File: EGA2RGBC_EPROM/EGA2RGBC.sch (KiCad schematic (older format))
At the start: 21 parts, among them J1 EGA Input, J3 CSync Selection, J4 Power, J5 Video Out, U1 27C010, U2 74LS244

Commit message: Update schematics
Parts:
- added JP2: Brown Fix, Connector_PinHeader_2.54mm:PinHeader_1x02_P2.54mm_Vertical, symbol Device:Jumper_NO_Small
- added R9: 4.7k, Resistor_THT:R_Axial_DIN0204_L3.6mm_D1.6mm_P7.62mm_Horizontal, symbol Device:R_Small
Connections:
- net GND: now also R9.1; no longer U1.26 (A9)
- net VCC: now also JP2.1
- new net: JP2.2, R9.2, U1.26 (A9)
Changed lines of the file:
@@
 $EndComp
-Wire Wire Line
-	2400 5750 2150 5750
-Wire Wire Line
-	2150 5750 2150 5850
 Wire Wire Line
 	2150 6450 2400 6450
 Wire Wire Line
 	2400 5850 2150 5850
-Connection ~ 2150 5850
 Wire Wire Line
 	2150 5850 2150 5950
@@
 	1    0    0    -1
 $EndComp
+$Comp
+L Device:R_Small R9
+U 1 1 6017B880
+P 1350 5750
+F 0 "R9" V 1400 5850 50  0000 C CNN
+F 1 "4.7k" V 1400 5600 50  0000 C CNN
+F 2 "Resistor_THT:R_Axial_DIN0204_L3.6mm_D1.6mm_P7.62mm_Horizontal" H 1350 5750 50  0001 C CNN
+F 3 "~" H 1350 5750 50  0001 C CNN
+	1    1350 5750
+	0    -1   -1   0
+$EndComp
+$Comp
+L Device:Jumper_NO_Small JP2
+U 1 1 6017DE7E
+P 1700 5950
+F 0 "JP2" H 1400 6050 50  0000 C CNN
+F 1 "Brown Fix" H 1700 6044 50  0000 C CNN
+F 2 "Connector_PinHeader_2.54mm:PinHeader_1x02_P2.54mm_Vertical" H 1700 5950 50  0001 C CNN
+F 3 "~" H 1700 5950 50  0001 C CNN
+	1    1700 5950
+	1    0    0    -1
+$EndComp
+Wire Wire Line
+	1050 4850 1050 5750
+Wire Wire Line
+	1050 5750 1250 5750
+Connection ~ 1050 4850
+Wire Wire Line
+	1450 5750 1950 5750
+Wire Wire Line
+	1800 5950 1950 5950
+Wire Wire Line
+	1950 5950 1950 5750
+Connection ~ 1950 5750
+Wire Wire Line
+	1950 5750 2400 5750
+$Comp
+L power:VCC #PWR?
+U 1 1 601AF6F5
+P 1350 5950
+F 0 "#PWR?" H 1350 5800 50  0001 C CNN
+F 1 "VCC" H 1365 6123 50  0000 C CNN
+F 2 "" H 1350 5950 50  0001 C CNN
+F 3 "" H 1350 5950 50  0001 C CNN
+	1    1350 5950
+	0    -1   -1   0
+$EndComp
+Wire Wire Line
+	1350 5950 1600 5950
 $EndSCHEMATC

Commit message: Create rev 1.1
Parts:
- C4, C5: footprint Capacitor_THT:C_Disc_D6.0mm_W2.5mm_P5.00mm -> Capacitor_THT:C_Disc_D3.0mm_W2.0mm_P2.50mm
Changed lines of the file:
@@
 Title ""
 Date ""
-Rev ""
+Rev "1.1"
 Comp ""
 Comment1 ""
@@
 F 0 "C4" H 6592 4296 50  0000 L CNN
 F 1 "100nF" H 6592 4205 50  0000 L CNN
-F 2 "Capacitor_THT:C_Disc_D6.0mm_W2.5mm_P5.00mm" H 6500 4250 50  0001 C CNN
+F 2 "Capacitor_THT:C_Disc_D3.0mm_W2.0mm_P2.50mm" H 6500 4250 50  0001 C CNN
 F 3 "~" H 6500 4250 50  0001 C CNN
 	1    6500 4250
@@
 F 0 "C5" H 7042 4296 50  0000 L CNN
 F 1 "100nF" H 7042 4205 50  0000 L CNN
-F 2 "Capacitor_THT:C_Disc_D6.0mm_W2.5mm_P5.00mm" H 6950 4250 50  0001 C CNN
+F 2 "Capacitor_THT:C_Disc_D3.0mm_W2.0mm_P2.50mm" H 6950 4250 50  0001 C CNN
 F 3 "~" H 6950 4250 50  0001 C CNN
 	1    6950 4250

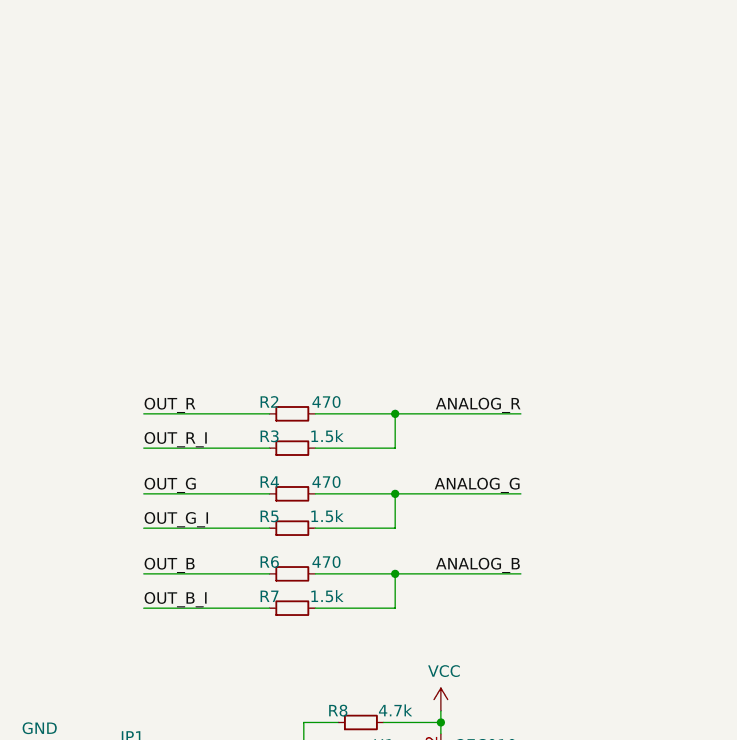
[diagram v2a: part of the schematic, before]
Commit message: Added caps on color lines
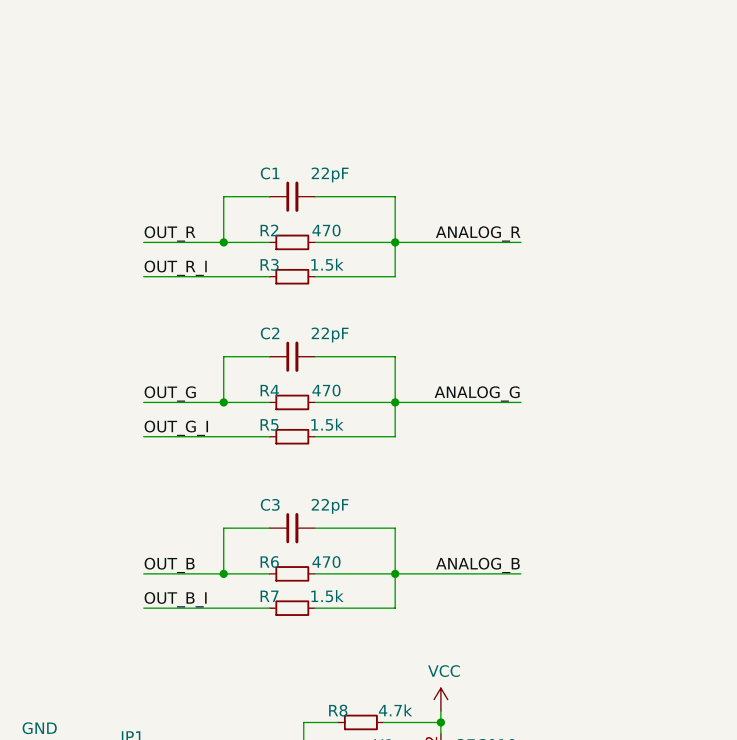
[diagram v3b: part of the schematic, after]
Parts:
- added C1, C2, C3: 22pF, Capacitor_THT:C_Disc_D3.0mm_W2.0mm_P2.50mm, symbol Device:C_Small
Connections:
- net ANALOG_B: now also C3.2
- net ANALOG_G: now also C2.2
- net ANALOG_R: now also C1.2
- net OUT_B: now also C3.1
- net OUT_G: now also C2.1
- net OUT_R: now also C1.1
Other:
- moved on the sheet: R2, R3, R4, R5
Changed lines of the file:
@@
 $EndComp
 Wire Wire Line
-	1500 3250 2050 3250
+	1500 2500 1850 2500
 $Comp
 L Device:R_Small R2
 U 1 1 5FC5E289
-P 2150 3250
-F 0 "R2" V 2200 3350 50  0000 C CNN
-F 1 "470" V 2200 3100 50  0000 C CNN
-F 2 "Resistor_THT:R_Axial_DIN0204_L3.6mm_D1.6mm_P7.62mm_Horizontal" H 2150 3250 50  0001 C CNN
-F 3 "~" H 2150 3250 50  0001 C CNN
-	1    2150 3250
-	0    -1   -1   0
-$EndComp
-Wire Wire Line
-	2250 3250 2600 3250
+P 2150 2500
+F 0 "R2" V 2200 2600 50  0000 C CNN
+F 1 "470" V 2200 2350 50  0000 C CNN
+F 2 "Resistor_THT:R_Axial_DIN0204_L3.6mm_D1.6mm_P7.62mm_Horizontal" H 2150 2500 50  0001 C CNN
+F 3 "~" H 2150 2500 50  0001 C CNN
+	1    2150 2500
+	0    -1   -1   0
+$EndComp
+Wire Wire Line
+	2250 2500 2600 2500
 $Comp
 L Device:R_Small R3
 U 1 1 5FC60558
-P 2150 3400
-F 0 "R3" V 2200 3500 50  0000 C CNN
-F 1 "1.5k" V 2200 3250 50  0000 C CNN
-F 2 "Resistor_THT:R_Axial_DIN0204_L3.6mm_D1.6mm_P7.62mm_Horizontal" H 2150 3400 50  0001 C CNN
-F 3 "~" H 2150 3400 50  0001 C CNN
-	1    2150 3400
-	0    -1   -1   0
-$EndComp
-Wire Wire Line
-	2250 3400 2600 3400
-Wire Wire Line
-	2600 3400 2600 3250
-Connection ~ 2600 3250
-Wire Wire Line
-	2600 3250 3150 3250
-Wire Wire Line
-	2050 3400 1500 3400
-Text Label 1500 3250 0    50   ~ 0
+P 2150 2650
+F 0 "R3" V 2200 2750 50  0000 C CNN
+F 1 "1.5k" V 2200 2500 50  0000 C CNN
+F 2 "Resistor_THT:R_Axial_DIN0204_L3.6mm_D1.6mm_P7.62mm_Horizontal" H 2150 2650 50  0001 C CNN
+F 3 "~" H 2150 2650 50  0001 C CNN
+	1    2150 2650
+	0    -1   -1   0
+$EndComp
+Wire Wire Line
+	2250 2650 2600 2650
+Wire Wire Line
+	2600 2650 2600 2500
+Connection ~ 2600 2500
+Wire Wire Line
+	2600 2500 3150 2500
+Wire Wire Line
+	2050 2650 1500 2650
+Text Label 1500 2500 0    50   ~ 0
 OUT_R
-Text Label 1500 3400 0    50   ~ 0
+Text Label 1500 2650 0    50   ~ 0
 OUT_R_I
-Text Label 3150 3250 2    50   ~ 0
+Text Label 3150 2500 2    50   ~ 0
 ANALOG_R
 Wire Wire Line
-	1500 3600 2050 3600
+	1500 3200 1850 3200
 $Comp
 L Device:R_Small R4
 U 1 1 5FC67AC6
-P 2150 3600
-F 0 "R4" V 2200 3700 50  0000 C CNN
-F 1 "470" V 2200 3450 50  0000 C CNN
-F 2 "Resistor_THT:R_Axial_DIN0204_L3.6mm_D1.6mm_P7.62mm_Horizontal" H 2150 3600 50  0001 C CNN
-F 3 "~" H 2150 3600 50  0001 C CNN
-	1    2150 3600
-	0    -1   -1   0
-$EndComp
-Wire Wire Line
-	2250 3600 2600 3600
+P 2150 3200
+F 0 "R4" V 2200 3300 50  0000 C CNN
+F 1 "470" V 2200 3050 50  0000 C CNN
+F 2 "Resistor_THT:R_Axial_DIN0204_L3.6mm_D1.6mm_P7.62mm_Horizontal" H 2150 3200 50  0001 C CNN
+F 3 "~" H 2150 3200 50  0001 C CNN
+	1    2150 3200
+	0    -1   -1   0
+$EndComp
+Wire Wire Line
+	2250 3200 2600 3200
 $Comp
 L Device:R_Small R5
 U 1 1 5FC67AD1
-P 2150 3750
-F 0 "R5" V 2200 3850 50  0000 C CNN
-F 1 "1.5k" V 2200 3600 50  0000 C CNN
-F 2 "Resistor_THT:R_Axial_DIN0204_L3.6mm_D1.6mm_P7.62mm_Horizontal" H 2150 3750 50  0001 C CNN
-F 3 "~" H 2150 3750 50  0001 C CNN
-	1    2150 3750
-	0    -1   -1   0
-$EndComp
-Wire Wire Line
-	2250 3750 2600 3750
-Wire Wire Line
-	2600 3750 2600 3600
-Connection ~ 2600 3600
-Wire Wire Line
-	2600 3600 3150 3600
-Wire Wire Line
-	2050 3750 1500 3750
-Text Label 1500 3600 0    50   ~ 0
+P 2150 3350
+F 0 "R5" V 2200 3450 50  0000 C CNN
+F 1 "1.5k" V 2200 3200 50  0000 C CNN
+F 2 "Resistor_THT:R_Axial_DIN0204_L3.6mm_D1.6mm_P7.62mm_Horizontal" H 2150 3350 50  0001 C CNN
+F 3 "~" H 2150 3350 50  0001 C CNN
+	1    2150 3350
+	0    -1   -1   0
+$EndComp
+Wire Wire Line
+	2250 3350 2600 3350
+Wire Wire Line
+	2600 3350 2600 3200
+Connection ~ 2600 3200
+Wire Wire Line
+	2600 3200 3150 3200
+Wire Wire Line
+	2050 3350 1500 3350
+Text Label 1500 3200 0    50   ~ 0
 OUT_G
-Text Label 1500 3750 0    50   ~ 0
+Text Label 1500 3350 0    50   ~ 0
 OUT_G_I
-Text Label 3150 3600 2    50   ~ 0
+Text Label 3150 3200 2    50   ~ 0
 ANALOG_G
 Wire Wire Line
-	1500 3950 2050 3950
+	1500 3950 1850 3950
 $Comp
 L Device:R_Small R6
@@
 Wire Wire Line
 	1350 5950 1600 5950
+$Comp
+L Device:C_Small C1
+U 1 1 611AF56D
+P 2150 2300
+F 0 "C1" V 2250 2350 50  0000 L CNN
+F 1 "22pF" V 2250 2050 50  0000 L CNN
+F 2 "Capacitor_THT:C_Disc_D3.0mm_W2.0mm_P2.50mm" H 2150 2300 50  0001 C CNN
+F 3 "~" H 2150 2300 50  0001 C CNN
+	1    2150 2300
+	0    -1   -1   0
+$EndComp
+Wire Wire Line
+	2250 2300 2600 2300
+Wire Wire Line
+	2600 2300 2600 2500
+Wire Wire Line
+	1850 2300 1850 2500
+Connection ~ 1850 2500
+Wire Wire Line
+	1850 2500 2050 2500
+Wire Wire Line
+	1850 2300 2050 2300
+$Comp
+L Device:C_Small C2
+U 1 1 611ECB00
+P 2150 3000
+F 0 "C2" V 2250 3050 50  0000 L CNN
+F 1 "22pF" V 2250 2750 50  0000 L CNN
+F 2 "Capacitor_THT:C_Disc_D3.0mm_W2.0mm_P2.50mm" H 2150 3000 50  0001 C CNN
+F 3 "~" H 2150 3000 50  0001 C CNN
+	1    2150 3000
+	0    -1   -1   0
+$EndComp
+Wire Wire Line
+	2250 3000 2600 3000
+Wire Wire Line
+	2600 3000 2600 3200
+Wire Wire Line
+	1850 3000 1850 3200
+Wire Wire Line
+	1850 3000 2050 3000
+Connection ~ 1850 3200
+Wire Wire Line
+	1850 3200 2050 3200
+$Comp
+L Device:C_Small C3
+U 1 1 61200708
+P 2150 3750
+F 0 "C3" V 2250 3800 50  0000 L CNN
+F 1 "22pF" V 2250 3500 50  0000 L CNN
+F 2 "Capacitor_THT:C_Disc_D3.0mm_W2.0mm_P2.50mm" H 2150 3750 50  0001 C CNN
+F 3 "~" H 2150 3750 50  0001 C CNN
+	1    2150 3750
+	0    -1   -1   0
+$EndComp
+Wire Wire Line
+	2250 3750 2600 3750
+Wire Wire Line
+	2600 3750 2600 3950
+Wire Wire Line
+	1850 3750 1850 3950
+Wire Wire Line
+	1850 3750 2050 3750
+Connection ~ 1850 3950
+Wire Wire Line
+	1850 3950 2050 3950
 $EndSCHEMATC

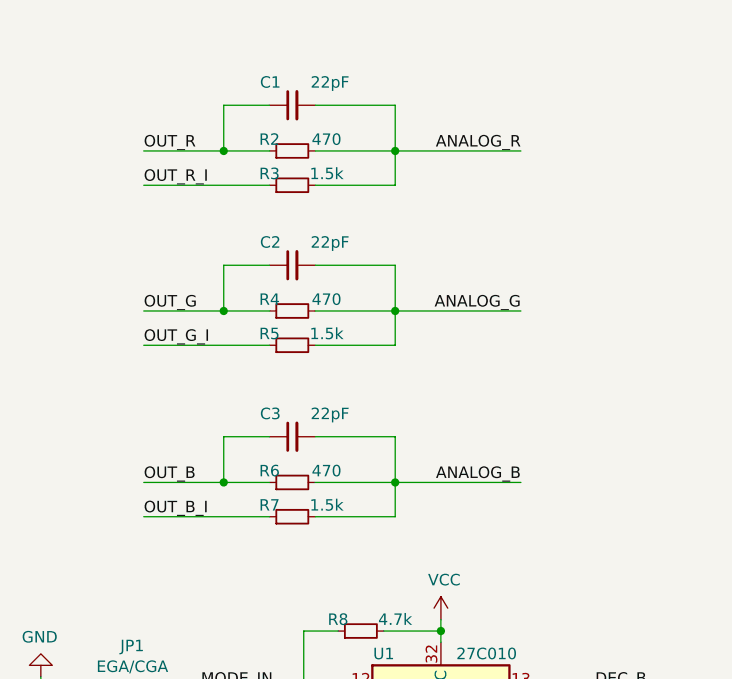
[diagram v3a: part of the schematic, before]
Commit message: Change some resistor values
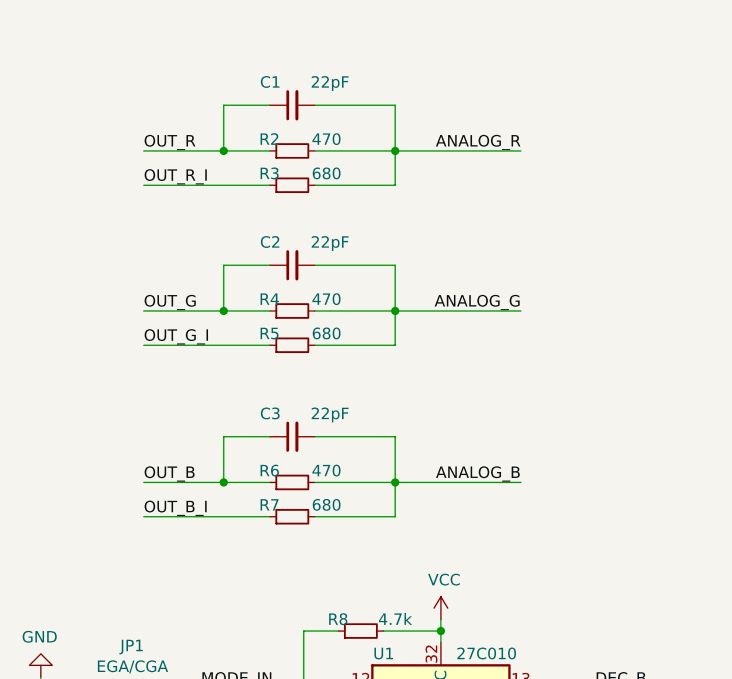
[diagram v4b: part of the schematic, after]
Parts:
- R3, R5, R7: value 1.5k -> 680
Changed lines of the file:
@@
 P 2150 2650
 F 0 "R3" V 2200 2750 50  0000 C CNN
-F 1 "1.5k" V 2200 2500 50  0000 C CNN
+F 1 "680" V 2200 2500 50  0000 C CNN
 F 2 "Resistor_THT:R_Axial_DIN0204_L3.6mm_D1.6mm_P7.62mm_Horizontal" H 2150 2650 50  0001 C CNN
 F 3 "~" H 2150 2650 50  0001 C CNN
@@
 P 2150 3350
 F 0 "R5" V 2200 3450 50  0000 C CNN
-F 1 "1.5k" V 2200 3200 50  0000 C CNN
+F 1 "680" V 2200 3200 50  0000 C CNN
 F 2 "Resistor_THT:R_Axial_DIN0204_L3.6mm_D1.6mm_P7.62mm_Horizontal" H 2150 3350 50  0001 C CNN
 F 3 "~" H 2150 3350 50  0001 C CNN
@@
 P 2150 4100
 F 0 "R7" V 2200 4200 50  0000 C CNN
-F 1 "1.5k" V 2200 3950 50  0000 C CNN
+F 1 "680" V 2200 3950 50  0000 C CNN
 F 2 "Resistor_THT:R_Axial_DIN0204_L3.6mm_D1.6mm_P7.62mm_Horizontal" H 2150 4100 50  0001 C CNN
 F 3 "~" H 2150 4100 50  0001 C CNN

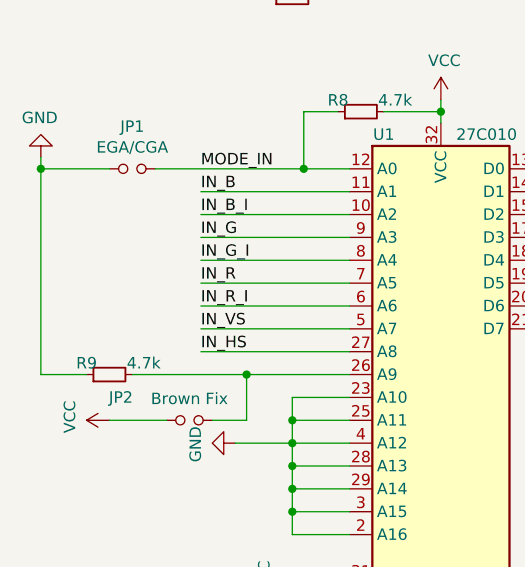
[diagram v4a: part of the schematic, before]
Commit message: Add pulldown resistor to inputs
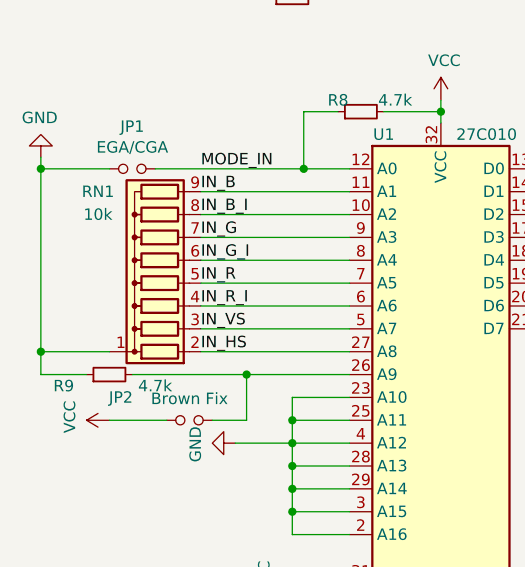
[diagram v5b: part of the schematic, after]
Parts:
- added RN1: 10k, Resistor_THT:R_Array_SIP9, symbol Device:R_Network08
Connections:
- net GND: now also RN1.1 (common)
- net IN_B: now also RN1.9 (R8)
- net IN_B_I: now also RN1.8 (R7)
- net IN_G: now also RN1.7 (R6)
- net IN_G_I: now also RN1.6 (R5)
- net IN_HS: now also RN1.2 (R1)
- net IN_R: now also RN1.5 (R4)
- net IN_R_I: now also RN1.4 (R3)
- net IN_VS: now also RN1.3 (R2)
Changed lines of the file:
@@
 U 1 1 6017B880
 P 1350 5750
-F 0 "R9" V 1400 5850 50  0000 C CNN
-F 1 "4.7k" V 1400 5600 50  0000 C CNN
+F 0 "R9" V 1300 5950 50  0000 C CNN
+F 1 "4.7k" V 1300 5550 50  0000 C CNN
 F 2 "Resistor_THT:R_Axial_DIN0204_L3.6mm_D1.6mm_P7.62mm_Horizontal" H 1350 5750 50  0001 C CNN
 F 3 "~" H 1350 5750 50  0001 C CNN
@@
 $EndComp
 Wire Wire Line
-	1050 4850 1050 5750
+	1050 4850 1050 5650
 Wire Wire Line
 	1050 5750 1250 5750
@@
 Wire Wire Line
 	1850 3950 2050 3950
+$Comp
+L Device:R_Network08 RN1
+U 1 1 61395436
+P 1550 5250
+F 0 "RN1" V 1850 5500 50  0000 C CNN
+F 1 "10k" V 1750 5500 50  0000 C CNN
+F 2 "Resistor_THT:R_Array_SIP9" V 2025 5250 50  0001 C CNN
+F 3 "http://www.vishay.com/docs/31509/csc.pdf" H 1550 5250 50  0001 C CNN
+	1    1550 5250
+	0    -1   -1   0
+$EndComp
+Wire Wire Line
+	1350 5650 1050 5650
+Connection ~ 1050 5650
+Wire Wire Line
+	1050 5650 1050 5750
 $EndSCHEMATC
